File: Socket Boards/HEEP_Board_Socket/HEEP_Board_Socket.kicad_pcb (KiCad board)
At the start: 4 copper layers, 64.9 x 71.4 mm, 70 parts

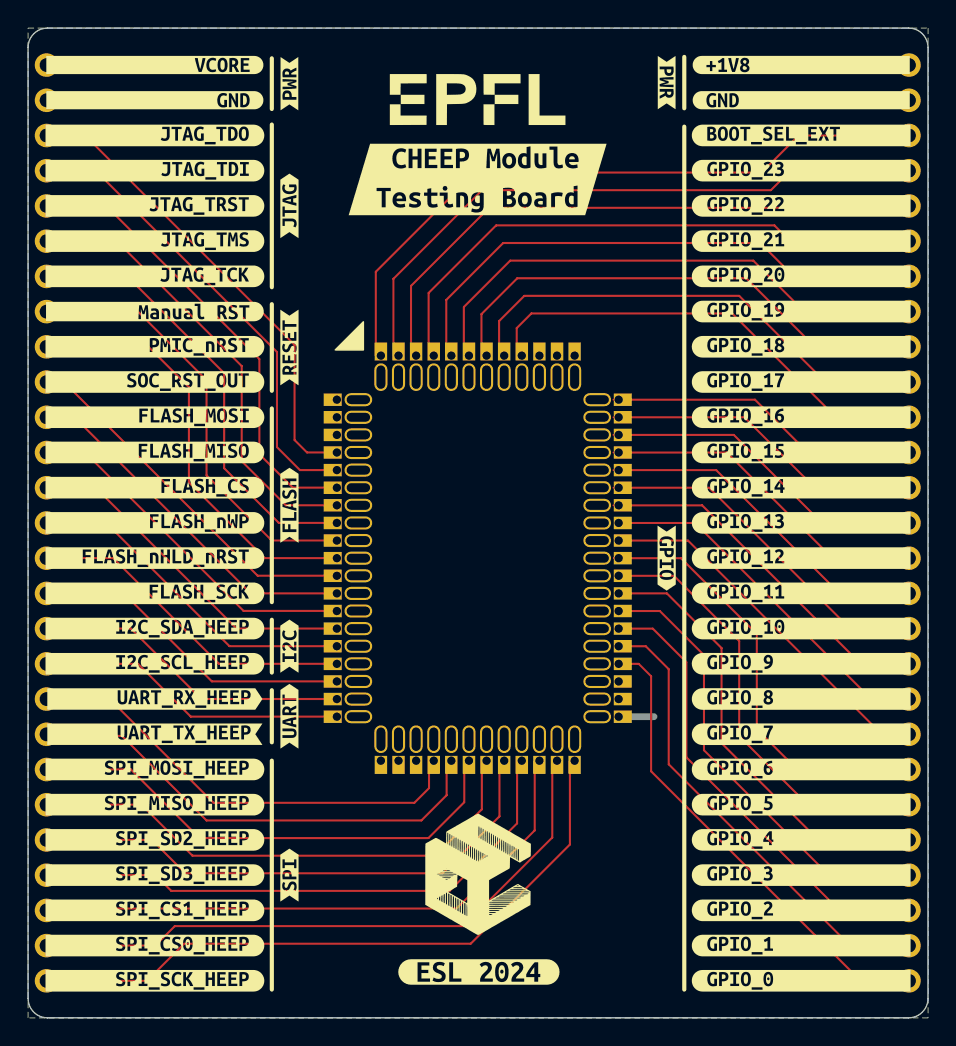
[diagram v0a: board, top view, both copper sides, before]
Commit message: Fixed paths of module boards
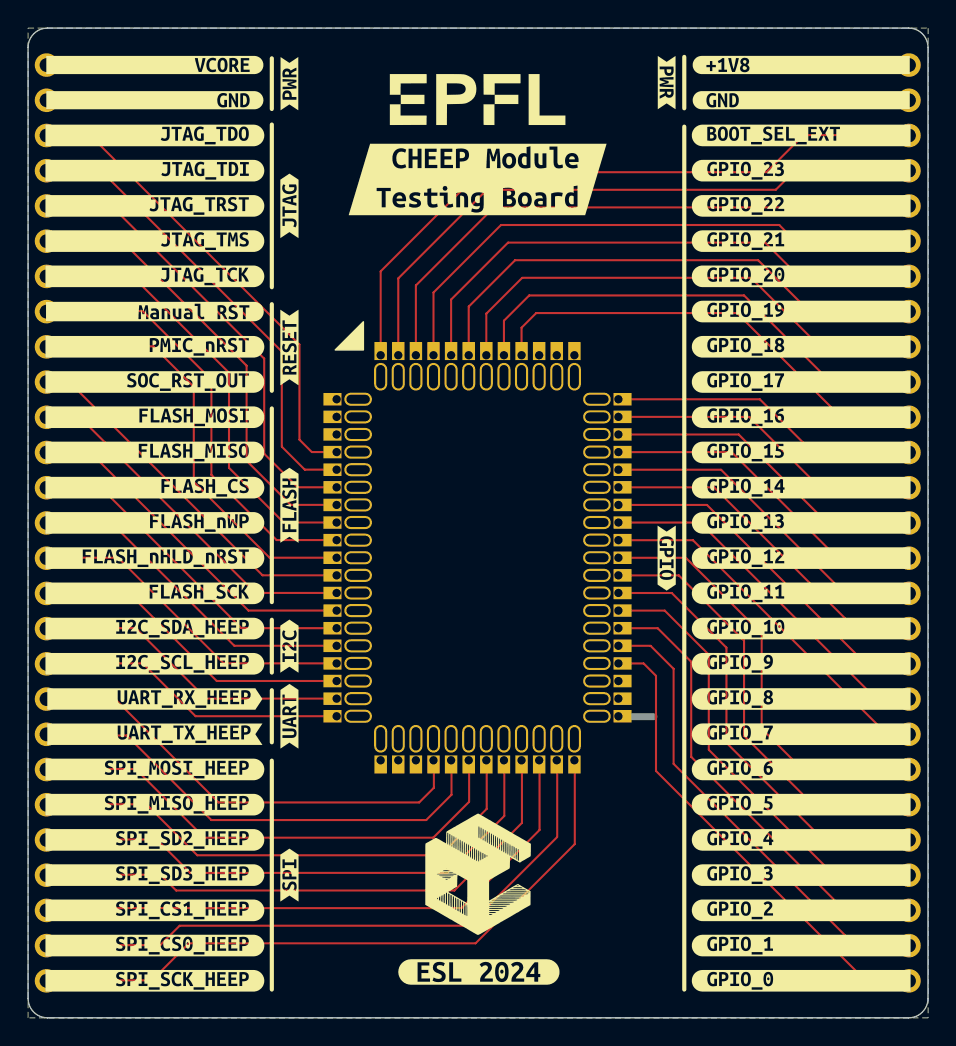
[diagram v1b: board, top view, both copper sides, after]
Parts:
- J1: footprint HeepoMind_PcbLib:HEEP_Board_Socket_Conn_1.27mm -> X-MODs_PcbLib:HEEP_Board_Socket_Conn_1.27mm
- J2: footprint HeepoMind_PcbLib:HEEP_Board_Header_Conn_1.27mm -> X-MODs_PcbLib:HEEP_Board_Header_Conn_1.27mm

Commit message: Fixed the castellated flexypins pad on the HEEP board socket
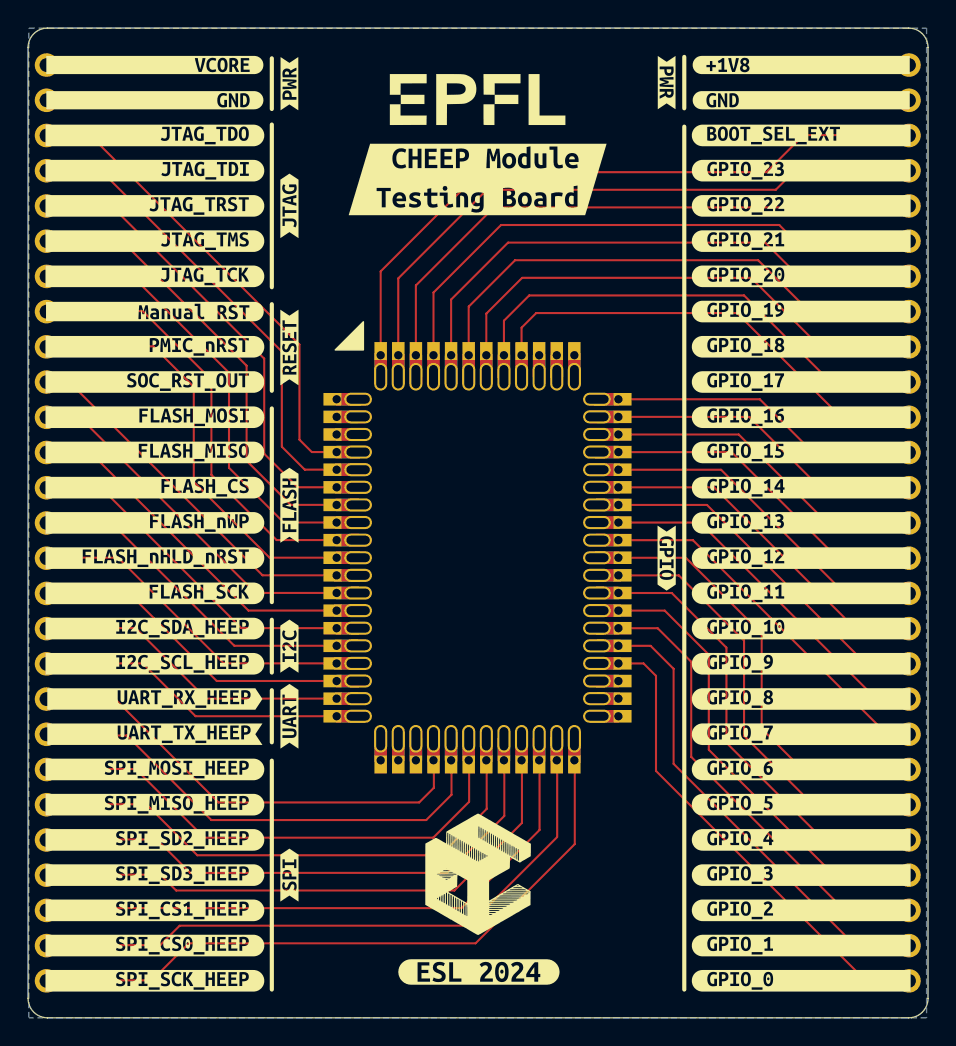
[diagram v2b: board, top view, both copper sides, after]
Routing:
- net VCORE: track 0.00 -> 24.8 mm
- net GND: track 0.00 -> 24.8 mm
- net +1V8: track 2.55 -> 24.8 mm
- net Net-(J1B-SPI_SD3_HEEP): track 40.5 -> 46.7 mm
- net Net-(J1C-GPIO_9): track 23.8 -> 30.0 mm
- net Net-(J1C-GPIO_23): track 34.0 -> 40.2 mm
- net Net-(J1C-GPIO_22): track 33.5 -> 39.7 mm
- net Net-(J1C-GPIO_21): track 33.0 -> 39.2 mm
- net Net-(J1C-GPIO_20): track 32.4 -> 38.6 mm
- net Net-(J1C-GPIO_19): track 32.2 -> 38.4 mm
- net Net-(J1C-GPIO_17): track 26.8 -> 33.0 mm
- net Net-(J1C-GPIO_15): track 26.3 -> 32.5 mm
- net Net-(J1C-GPIO_14): track 25.8 -> 32.0 mm
- net Net-(J1C-GPIO_13): track 25.3 -> 31.5 mm
- net Net-(J1C-GPIO_12): track 24.5 -> 30.7 mm
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
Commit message: Added via stitching to the socket boards
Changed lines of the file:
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@@
-	)
-	(segment
-		(start 112.364427 124.81183)
-		(end 112.110427 125.06583)
-		(width 0.15)
-		(layer "F.Cu")
-		(net 43)
 	)
 	(segment
